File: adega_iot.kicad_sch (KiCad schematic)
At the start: 65 parts, among them J1 Conn_01x03_Pin, J10 Conn_01x02_Pin, J2 Conn_01x02_Pin, J3 Screw_Terminal_01x02, J4 Conn_01x03_Pin, J6 Conn_01x03_Pin, J7 Screw_Terminal_01x02, J8 Conn_01x02_Pin, J9 Conn_01x02_Pin, Q1 BC548, Q10 BC548, Q11 BC558, Q12 IRF540N, Q13 IRF540N, Q2 IRF540N, Q3 IRF540N, Q4 BC548, Q5 BC558, Q6 BC548, Q7 BC548, Q8 BC548, Q9 BC558, SW1 SW_Push, SW2 SW_Push, U1 LM324, U2 ESP32-DevKitC, U3 YAAJ_DCDC_StepDown_LM2596

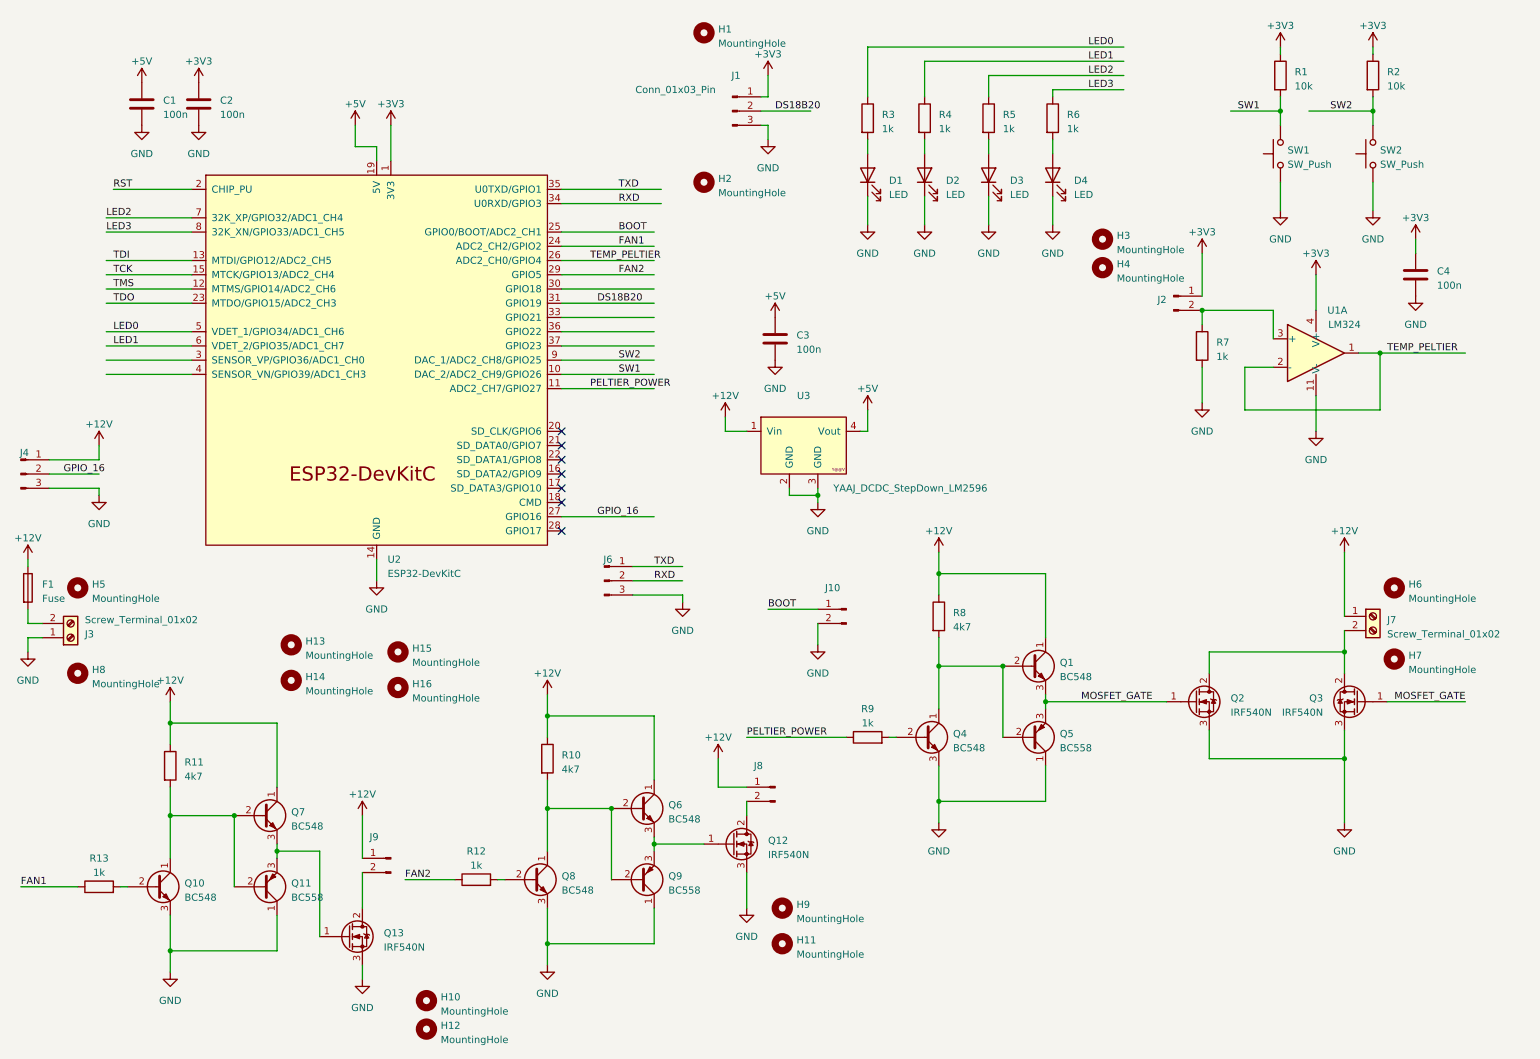
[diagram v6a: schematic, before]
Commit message: Reset Button and NTC pullup
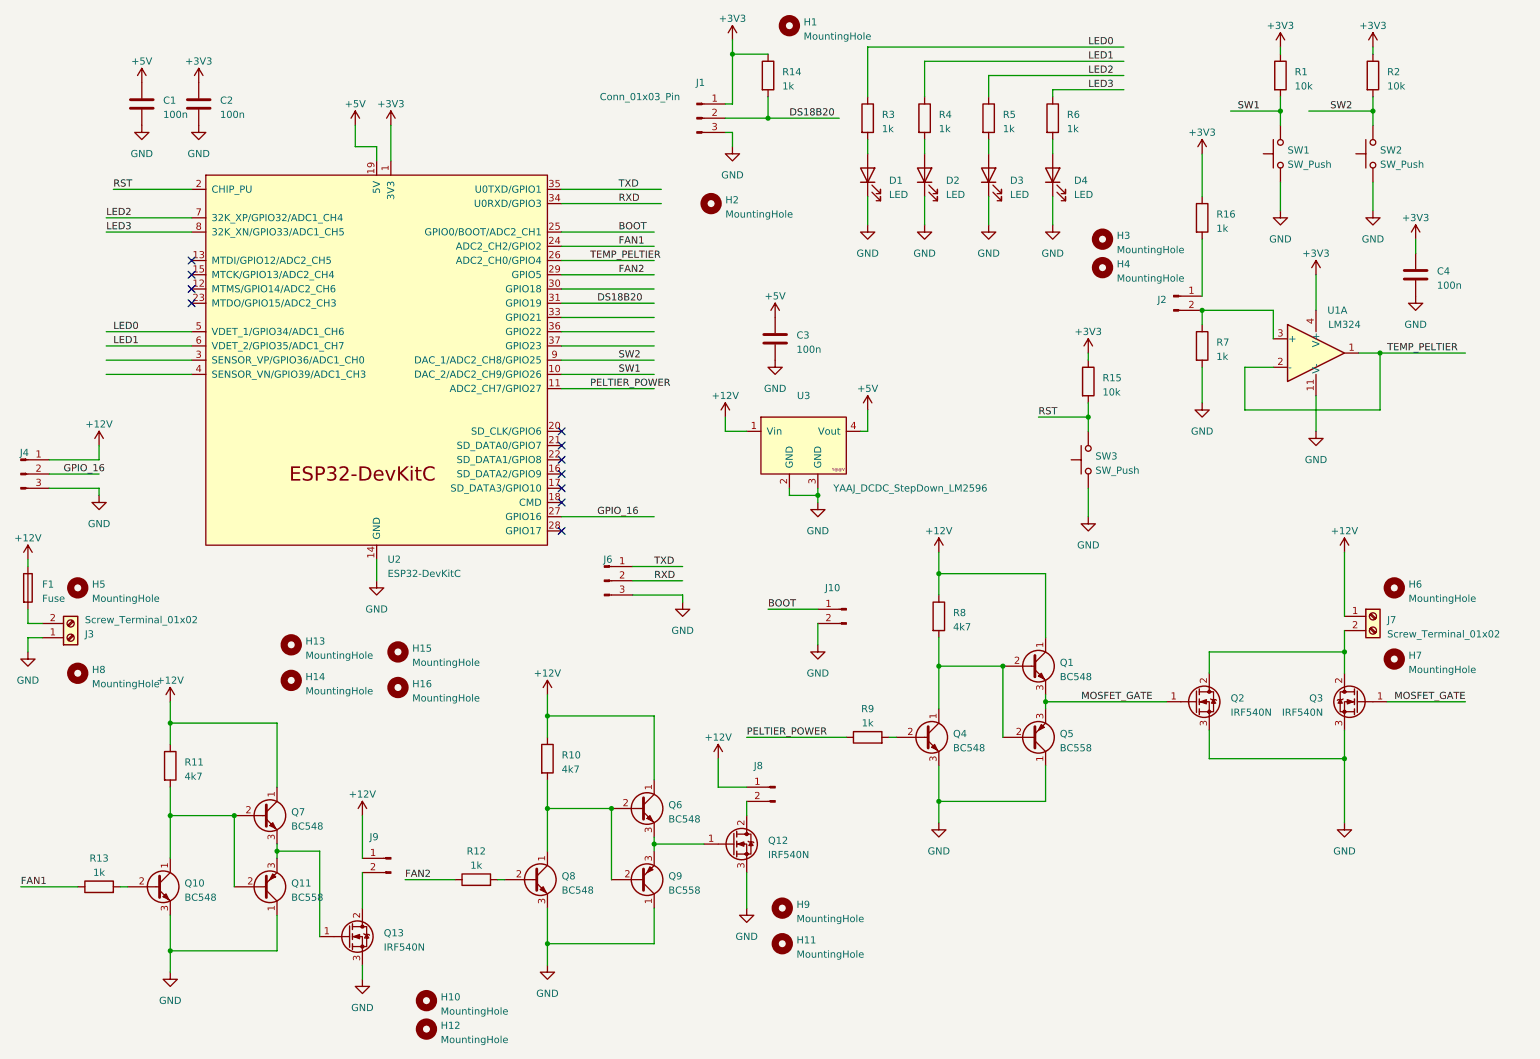
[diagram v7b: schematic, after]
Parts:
- added R14, R16: 1k, Resistor_THT:R_Axial_DIN0204_L3.6mm_D1.6mm_P7.62mm_Horizontal, symbol Device:R
- added R15: 10k, Resistor_THT:R_Axial_DIN0204_L3.6mm_D1.6mm_P7.62mm_Horizontal, symbol Device:R
- added SW3: SW_Push, Button_Switch_THT:SW_PUSH_6mm_H7.3mm, symbol Switch:SW_Push
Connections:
- net +3V3: now also R14.1, R15.1, R16.1; no longer J2.1 (Pin_1)
- net DS18B20: now also R14.2
- net GND: now also SW3.1
- net RST: now also R15.2, SW3.2
- net TCK: no longer names the net of U2.15 (MTCK/GPIO13/ADC2_CH4)
- net TDI: no longer names the net of U2.13 (MTDI/GPIO12/ADC2_CH5)
- net TDO: no longer names the net of U2.23 (MTDO/GPIO15/ADC2_CH3)
- net TMS: no longer names the net of U2.12 (MTMS/GPIO14/ADC2_CH6)
- new net: J2.1 (Pin_1), R16.2
- no-connect marks 7 -> 11
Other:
- moved on the sheet: H1, H2, J1

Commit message: Added Thermistor on GPIO pin
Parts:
- removed J10: Conn_01x02_Pin, Connector_PinHeader_2.54mm:PinHeader_1x02_P2.54mm_Vertical, symbol Connector:Conn_01x02_Pin
- removed R15: 10k, Resistor_THT:R_Axial_DIN0204_L3.6mm_D1.6mm_P7.62mm_Horizontal, symbol Device:R
- removed SW3: SW_Push, Button_Switch_THT:SW_PUSH_6mm_H7.3mm, symbol Switch:SW_Push
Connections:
- net +3V3: no longer R16.1
- net THERMISTOR_ON: now reaches U2.33 (GPIO21)
- net THERMISTOR_ON: now also R16.1
- net RST: no longer names the net of U2.2 (CHIP_PU)
- no-connect marks 11 -> 14
